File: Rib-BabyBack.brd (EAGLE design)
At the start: 67.3 x 74.9 mm, 25 parts, among them IC1 REG1117, SW1 DPDT

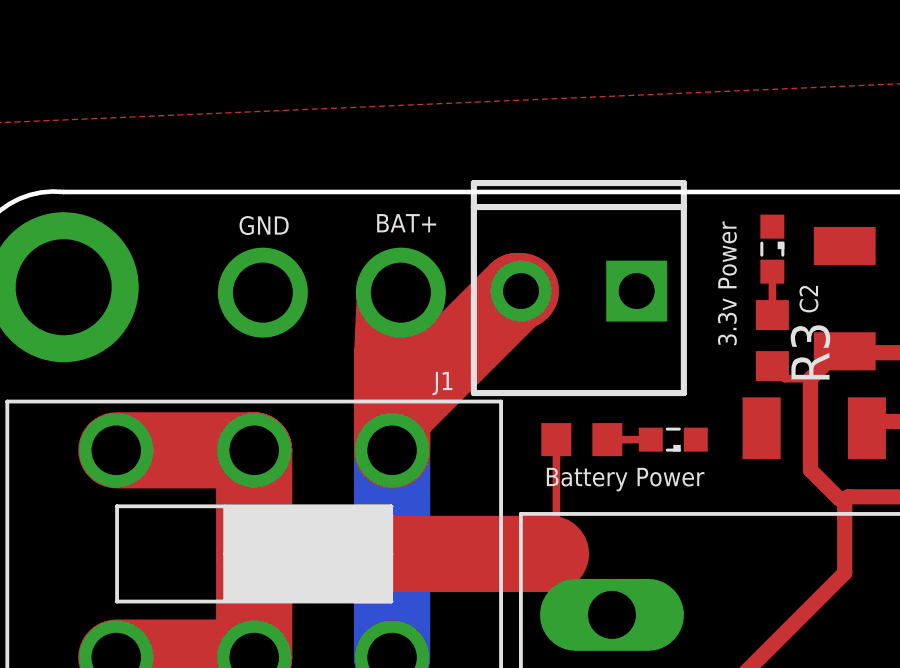
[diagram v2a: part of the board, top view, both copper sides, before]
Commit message: Issue #22 Solder lugs resized to 3MM diameter holes and moved
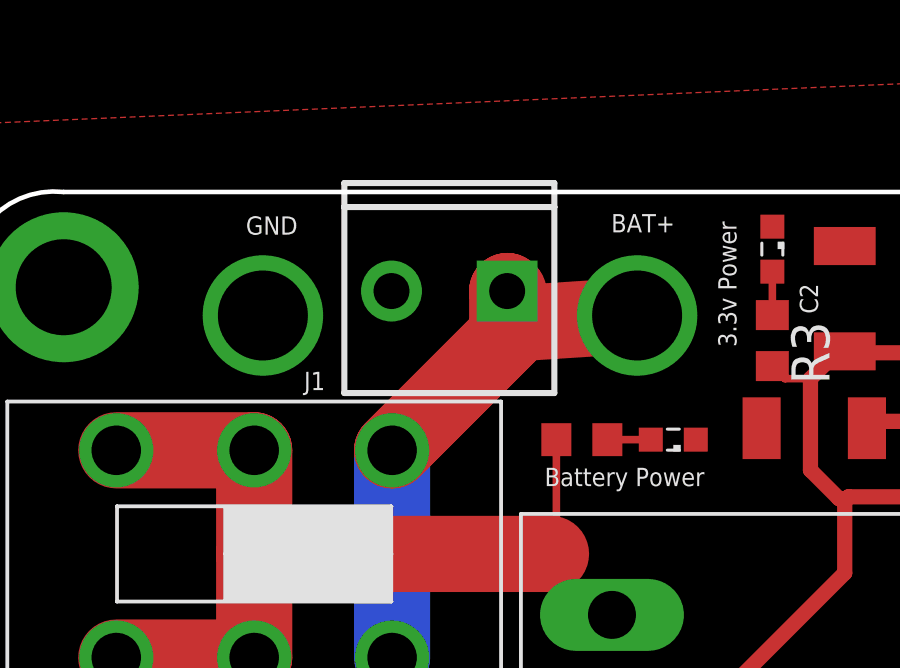
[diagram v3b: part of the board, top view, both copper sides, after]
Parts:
- moved J1 4.32 mm to (18.2, 72.3)
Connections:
- net GND: now also J1.2; no longer J1.1
- net N$11: now also J1.1; no longer J1.2
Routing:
- net N$11: track 19.8 -> 23.8 mm
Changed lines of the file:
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@@
 <text x="64.8208" y="56.6928" size="0.6096" layer="21" font="vector" ratio="20" rot="R90">GND</text>
 <text x="62.23" y="56.6928" size="0.6096" layer="21" font="vector" ratio="20" rot="R90">BAT+</text>
-<text x="16.0528" y="74.8284" size="0.6096" layer="21" font="vector" ratio="20" rot="R180">BAT+</text>
-<text x="11.0998" y="74.7522" size="0.6096" layer="21" font="vector" ratio="20" rot="R180">GND</text>
+<text x="23.9268" y="74.8284" size="0.6096" layer="21" font="vector" ratio="20" rot="R180">BAT+</text>
+<text x="11.3538" y="74.7522" size="0.6096" layer="21" font="vector" ratio="20" rot="R180">GND</text>
 <text x="39.9796" y="74.1426" size="0.6096" layer="21" font="vector" ratio="20" align="center">WII
 ACCESSORY</text>
@@
 </element>
 <element name="SW1" library="GF-126-0327" package="GF-126-0327" value="DPDT" x="9.906" y="63.5" smashed="yes"/>
-<element name="J1" library="SparkFun-Connectors" package="SCREWTERMINAL-3.5MM-2_LOCK" value="" x="22.479" y="72.263" smashed="yes" rot="R180">
-<attribute name="NAME" x="16.5862" y="69.5706" size="0.6096" layer="25" font="vector" ratio="20" rot="R180"/>
-<attribute name="PROD_ID" value="CONN-08399" x="22.479" y="72.263" size="1.778" layer="27" rot="R180" display="off"/>
-<attribute name="VALUE" x="23.749" y="70.993" size="0.6096" layer="27" font="vector" ratio="20" rot="R180"/>
+<element name="J1" library="SparkFun-Connectors" package="SCREWTERMINAL-3.5MM-2_LOCK" value="" x="18.161" y="72.263" smashed="yes" rot="R180">
+<attribute name="NAME" x="12.2682" y="69.5706" size="0.6096" layer="25" font="vector" ratio="20" rot="R180"/>
+<attribute name="PROD_ID" value="CONN-08399" x="18.161" y="72.263" size="1.778" layer="27" rot="R180" display="off"/>
+<attribute name="VALUE" x="19.431" y="70.993" size="0.6096" layer="27" font="vector" ratio="20" rot="R180"/>
 </element>
 <element name="F4" library="3557-2" package="3557-2" value="3557-2" x="28.702" y="61.468"/>
@@
 <wire x1="51.531" y1="71.315" x2="51.562" y2="71.284" width="0.254" layer="1"/>
 <wire x1="51.562" y1="71.284" x2="51.562" y2="66.929" width="0.254" layer="1"/>
-<contactref element="J1" pad="1"/>
-<via x="10.196" y="72.21" extent="1-16" drill="2"/>
+<via x="10.196" y="71.448" extent="1-16" drill="3"/>
 <contactref element="LED3" pad="C"/>
 <contactref element="LED2" pad="C"/>
 <contactref element="LED1" pad="C"/>
 <contactref element="LED4" pad="C"/>
+<contactref element="J1" pad="2"/>
 </signal>
 <signal name="N$12">
@@
 <contactref element="SW1" pad="C2"/>
 <contactref element="SW1" pad="C1"/>
-<wire x1="14.5034" y1="68.0974" x2="14.5034" y2="66.9544" width="2.54" layer="1"/>
 <wire x1="14.5034" y1="60.0456" x2="14.5034" y2="66.9544" width="2.54" layer="16"/>
-<contactref element="J1" pad="2"/>
-<wire x1="18.669" y1="72.263" x2="18.8012" y2="72.263" width="2.54" layer="1"/>
-<wire x1="14.5034" y1="68.0974" x2="18.669" y2="72.263" width="2.54" layer="1"/>
-<wire x1="14.5034" y1="66.9544" x2="14.5034" y2="70.1026" width="2.54" layer="1"/>
-<wire x1="14.5034" y1="70.1026" x2="14.596" y2="72.21" width="2.54" layer="1"/>
-<wire x1="14.596" y1="72.21" x2="14.796" y2="72.21" width="2.54" layer="1"/>
-<via x="14.796" y="72.21" extent="1-16" drill="2"/>
-<wire x1="14.796" y1="72.21" x2="14.996" y2="72.01" width="2.54" layer="16"/>
+<via x="22.67" y="71.448" extent="1-16" drill="3"/>
+<contactref element="J1" pad="1"/>
+<wire x1="18.3918" y1="72.21" x2="18.3388" y2="72.263" width="2.54" layer="1"/>
+<wire x1="18.3388" y1="72.263" x2="18.3388" y2="70.7898" width="2.54" layer="1"/>
+<wire x1="18.3388" y1="70.7898" x2="14.5034" y2="66.9544" width="2.54" layer="1"/>
+<wire x1="22.67" y1="71.448" x2="18.743" y2="71.194" width="2.54" layer="1"/>
+<wire x1="18.743" y1="71.194" x2="14.5034" y2="66.9544" width="2.54" layer="1"/>
 </signal>
 <signal name="DET">

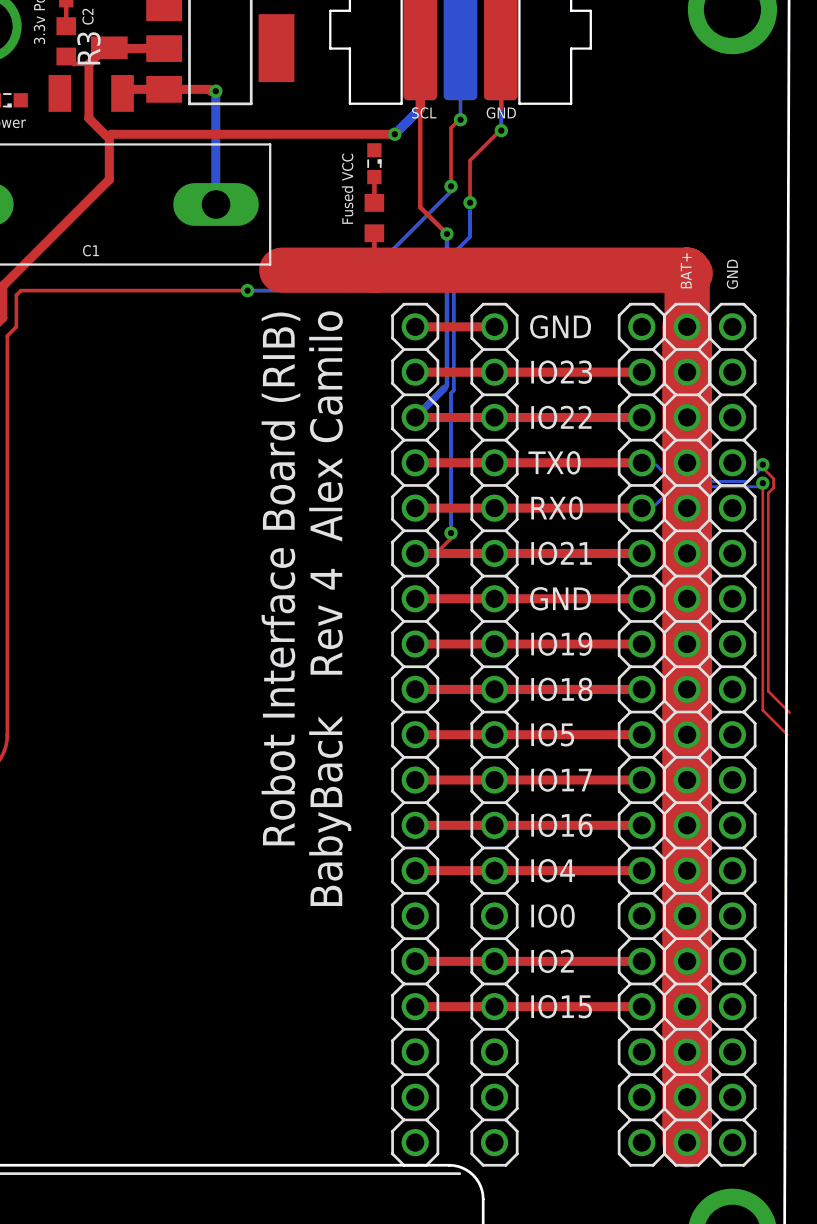
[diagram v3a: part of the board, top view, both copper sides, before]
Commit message: Issue #19 4k7 ohm pullups to 3.3v are needed on SDA and SCL
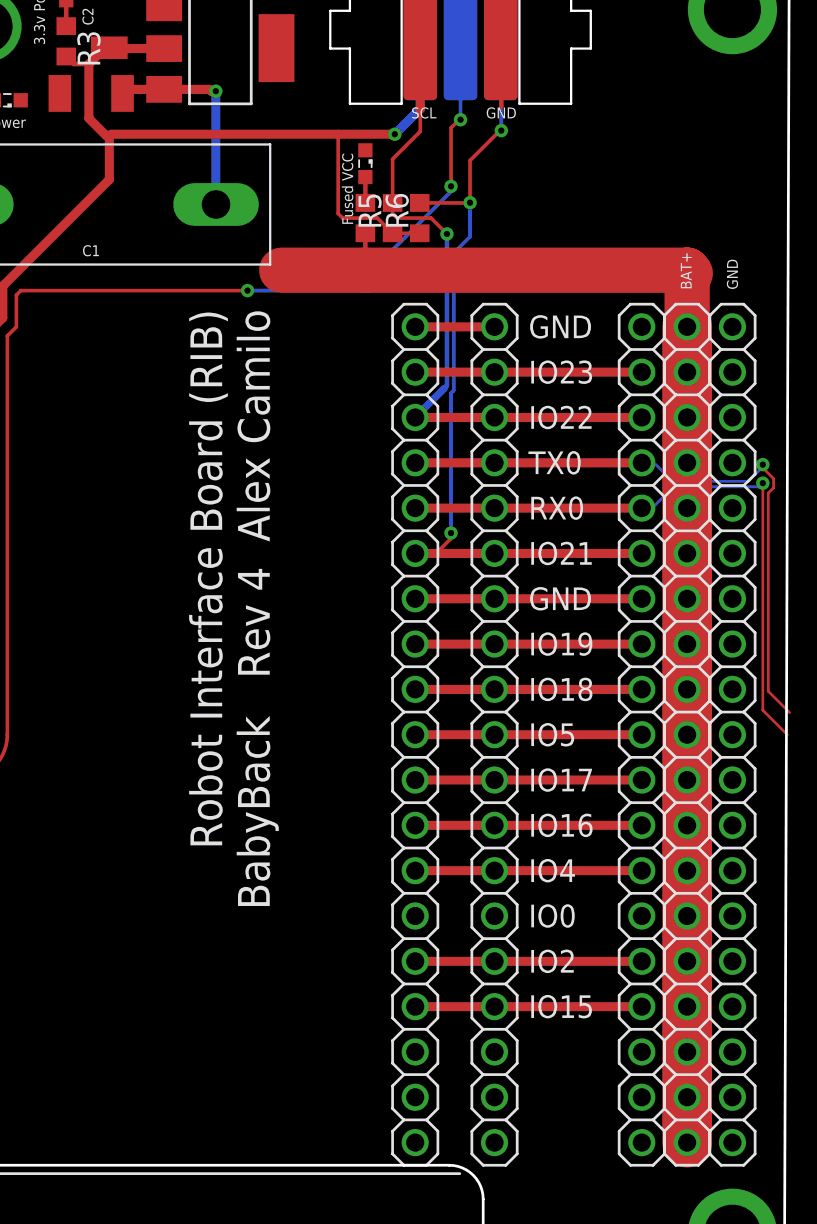
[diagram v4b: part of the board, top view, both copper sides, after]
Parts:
- added R5, R6: (no value), resistor:R0603
- moved LED1 0.51 mm to (43.9, 63.8)
- moved R1 0.51 mm to (43.9, 60.7)
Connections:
- net SCL: now also R5.2
- net SDA: now also R6.2
- net V3.3: now also R5.1, R6.1
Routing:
- net V3.3: track 110.0 -> 119.5 mm
- net SDA: track 42.7 -> 45.6 mm
- net SCL: track 31.8 -> 34.2 mm
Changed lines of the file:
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@@
 <wire x1="49.236" y1="7.15" x2="49.236" y2="56.35" width="0.1524" layer="22"/>
 <wire x1="49.236" y1="56.35" x2="18.796" y2="56.35" width="0.1524" layer="22"/>
-<text x="38.2016" y="55.6006" size="1.778" layer="21" font="vector" ratio="20" rot="R270">Robot Interface Board (RIB)
+<text x="34.1376" y="55.6006" size="1.778" layer="21" font="vector" ratio="20" rot="R270">Robot Interface Board (RIB)
 BabyBack   Rev 4  Alex Camilo</text>
 <wire x1="0.381" y1="3.175" x2="2.921" y2="0.635" width="0.1524" layer="20" curve="90"/>
@@
 </element>
 <element name="F4" library="3557-2" package="3557-2" value="3557-2" x="28.702" y="61.468"/>
-<element name="LED1" library="eagle-ltspice" library_urn="urn:adsk.eagle:library:217" package="LED_SML0603" package3d_urn="urn:adsk.eagle:package:13315/1" value="" x="44.45" y="63.754" smashed="yes" rot="R270">
-<attribute name="SPICEMODEL" value="NONE" x="44.45" y="63.754" size="1.778" layer="27" rot="R270" display="off"/>
-<attribute name="SPICEPREFIX" value="D" x="44.45" y="63.754" size="1.778" layer="27" rot="R270" display="off"/>
-<attribute name="SPICETYPE" value="diode" x="44.45" y="63.754" size="1.778" layer="27" rot="R270" display="off"/>
-<attribute name="VALUE" x="42.45" y="64.754" size="1.27" layer="27" rot="R270"/>
+<element name="LED1" library="eagle-ltspice" library_urn="urn:adsk.eagle:library:217" package="LED_SML0603" package3d_urn="urn:adsk.eagle:package:13315/1" value="" x="43.942" y="63.754" smashed="yes" rot="R270">
+<attribute name="SPICEMODEL" value="NONE" x="43.942" y="63.754" size="1.778" layer="27" rot="R270" display="off"/>
+<attribute name="SPICEPREFIX" value="D" x="43.942" y="63.754" size="1.778" layer="27" rot="R270" display="off"/>
+<attribute name="SPICETYPE" value="diode" x="43.942" y="63.754" size="1.778" layer="27" rot="R270" display="off"/>
+<attribute name="VALUE" x="41.942" y="64.754" size="1.27" layer="27" rot="R270"/>
 </element>
 <element name="LED2" library="eagle-ltspice" library_urn="urn:adsk.eagle:library:217" package="LED_SML0603" package3d_urn="urn:adsk.eagle:package:13315/1" value="" x="23.876" y="67.31" smashed="yes" rot="R180">
@@
 <attribute name="VALUE" x="25.178" y="74.66" size="1.27" layer="27" rot="R270"/>
 </element>
-<element name="R1" library="resistor" library_urn="urn:adsk.eagle:library:348" package="R0603" package3d_urn="urn:adsk.eagle:package:26057/1" value="" x="44.45" y="60.706" smashed="yes" rot="R270">
-<attribute name="VALUE" x="42.545" y="61.341" size="1.27" layer="27" rot="R270"/>
+<element name="R1" library="resistor" library_urn="urn:adsk.eagle:library:348" package="R0603" package3d_urn="urn:adsk.eagle:package:26057/1" value="" x="43.942" y="60.706" smashed="yes" rot="R270">
+<attribute name="VALUE" x="42.037" y="61.341" size="1.27" layer="27" rot="R270"/>
 </element>
 <element name="R2" library="resistor" library_urn="urn:adsk.eagle:library:348" package="R0603" package3d_urn="urn:adsk.eagle:package:26057/1" value="" x="20.828" y="67.31" smashed="yes" rot="R180">
@@
 </element>
 <element name="R4" library="resistor" library_urn="urn:adsk.eagle:library:348" package="R0603" package3d_urn="urn:adsk.eagle:package:26057/1" value="" x="12.954" y="16.256" rot="R90"/>
+<element name="R5" library="resistor" library_urn="urn:adsk.eagle:library:348" package="R0603" package3d_urn="urn:adsk.eagle:package:26057/1" value="" x="45.466" y="60.706" rot="R90"/>
+<element name="R6" library="resistor" library_urn="urn:adsk.eagle:library:348" package="R0603" package3d_urn="urn:adsk.eagle:package:26057/1" value="" x="46.99" y="60.706" rot="R90"/>
 </elements>
 <signals>
@@
 <contactref element="LED4" pad="C"/>
 <contactref element="J1" pad="2"/>
+<wire x1="43.942" y1="64.504" x2="51.562" y2="66.929" width="0" layer="19" extent="1-1"/>
 </signal>
 <signal name="N$12">
@@
 <wire x1="61.976" y1="57.785" x2="61.976" y2="54.61" width="2.54" layer="1"/>
 <wire x1="61.976" y1="57.785" x2="62.1538" y2="57.6072" width="2.54" layer="1"/>
-<wire x1="39.255" y1="57.785" x2="44.45" y2="57.785" width="2.54" layer="1"/>
+<wire x1="39.255" y1="57.785" x2="43.942" y2="57.785" width="2.54" layer="1"/>
 <contactref element="F4" pad="P$1"/>
-<wire x1="44.45" y1="57.785" x2="61.976" y2="57.785" width="2.54" layer="1"/>
+<wire x1="43.942" y1="57.785" x2="61.976" y2="57.785" width="2.54" layer="1"/>
 <wire x1="32.6644" y1="67.9196" x2="35.2044" y2="67.9196" width="0.508" layer="1"/>
 <wire x1="35.2044" y1="67.9196" x2="35.306" y2="67.818" width="0.508" layer="1"/>
@@
 <wire x1="30.5586" y1="67.9196" x2="30.33" y2="67.691" width="0.508" layer="1"/>
 <contactref element="R1" pad="2"/>
-<wire x1="44.45" y1="59.856" x2="44.45" y2="57.785" width="0.254" layer="1"/>
+<wire x1="43.942" y1="59.856" x2="43.942" y2="57.785" width="0.254" layer="1"/>
 <wire x1="61.976" y1="49.53" x2="61.976" y2="52.07" width="0" layer="19" extent="1-1"/>
 <wire x1="61.976" y1="46.99" x2="61.976" y2="49.53" width="0" layer="19" extent="1-1"/>
@@
 <wire x1="48.895" y1="58.7502" x2="49.8094" y2="59.6646" width="0.2032" layer="16"/>
 <wire x1="49.8094" y1="59.6646" x2="49.8094" y2="61.5696" width="0.2032" layer="16"/>
+<contactref element="R6" pad="2"/>
+<wire x1="46.99" y1="61.556" x2="49.7958" y2="61.556" width="0.2032" layer="1"/>
+<wire x1="49.7958" y1="61.556" x2="49.8094" y2="61.5696" width="0.2032" layer="1"/>
 <wire x1="51.562" y1="67.437" x2="51.435" y2="69.596" width="0" layer="19" extent="16-16"/>
 </signal>
@@
 <wire x1="48.514" y1="51.308" x2="48.514" y2="59.817" width="0.254" layer="16"/>
 <via x="48.514" y="59.817" extent="1-16" drill="0.35"/>
-<wire x1="48.514" y1="59.817" x2="47.021" y2="61.31" width="0.254" layer="1"/>
-<wire x1="47.021" y1="61.31" x2="47.021" y2="66.802" width="0.254" layer="1"/>
 <wire x1="47.021" y1="66.802" x2="47.021" y2="67.2846" width="0.508" layer="1"/>
+<contactref element="R5" pad="2"/>
+<wire x1="48.514" y1="59.817" x2="47.625" y2="60.706" width="0.2032" layer="1"/>
+<wire x1="45.72" y1="60.706" x2="45.466" y2="60.96" width="0.2032" layer="1"/>
+<wire x1="45.466" y1="60.96" x2="45.466" y2="61.556" width="0.2032" layer="1"/>
+<wire x1="47.625" y1="60.706" x2="45.72" y2="60.706" width="0.2032" layer="1"/>
+<wire x1="45.466" y1="61.556" x2="45.466" y2="64.008" width="0.2032" layer="1"/>
+<wire x1="45.466" y1="64.008" x2="47.021" y2="65.563" width="0.2032" layer="1"/>
+<wire x1="47.021" y1="65.563" x2="47.021" y2="66.802" width="0.2032" layer="1"/>
 <wire x1="47.021" y1="67.2846" x2="47.021" y2="71.315" width="0" layer="19" extent="1-1"/>
 </signal>
@@
 <wire x1="29.718" y1="65.405" x2="29.6545" y2="65.3415" width="0.508" layer="1"/>
 <wire x1="29.6545" y1="65.3415" x2="29.591" y2="65.278" width="0.508" layer="1"/>
-<wire x1="45.593" y1="65.405" x2="29.718" y2="65.405" width="0.508" layer="1"/>
+<wire x1="45.593" y1="65.405" x2="42.418" y2="65.405" width="0.508" layer="1"/>
+<wire x1="42.418" y1="65.405" x2="29.718" y2="65.405" width="0.508" layer="1"/>
 <wire x1="29.6545" y1="65.3415" x2="29.4005" y2="65.3415" width="0.508" layer="1"/>
 <wire x1="29.4005" y1="65.3415" x2="28.448" y2="66.294" width="0.508" layer="1"/>
@@
 <wire x1="23.622" y1="56.896" x2="29.591" y2="62.865" width="0.508" layer="1"/>
 <wire x1="29.591" y1="62.865" x2="29.591" y2="65.278" width="0.508" layer="1"/>
+<contactref element="R6" pad="1"/>
+<contactref element="R5" pad="1"/>
+<wire x1="46.99" y1="59.856" x2="45.466" y2="59.856" width="0.2032" layer="1"/>
+<wire x1="45.466" y1="59.856" x2="44.616" y2="60.706" width="0.2032" layer="1"/>
+<wire x1="44.616" y1="60.706" x2="42.672" y2="60.706" width="0.2032" layer="1"/>
+<wire x1="42.672" y1="60.706" x2="42.418" y2="60.96" width="0.2032" layer="1"/>
+<wire x1="42.418" y1="60.96" x2="42.418" y2="65.405" width="0.2032" layer="1"/>
 <wire x1="6.096" y1="49.53" x2="6.096" y2="52.07" width="0" layer="19" extent="1-1"/>
 <wire x1="6.096" y1="46.99" x2="6.096" y2="49.53" width="0" layer="19" extent="1-1"/>
@@
 <contactref element="R1" pad="1"/>
 <contactref element="LED1" pad="A"/>
-<wire x1="44.45" y1="61.556" x2="44.45" y2="63.004" width="0.254" layer="1"/>
+<wire x1="43.942" y1="61.556" x2="43.942" y2="63.004" width="0.254" layer="1"/>
 </signal>
 <signal name="N$37">
